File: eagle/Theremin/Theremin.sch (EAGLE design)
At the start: 50 parts, among them Q1 2N3904, Q2 2N3904, Q6 2N3904, Q7 2N3904, Q8 2N3904, U1 LM78L12, U2 LM79L12

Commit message: Work on VOLTAGE CONTROLLED AMPLIFIER section
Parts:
- added C25: 1uF, SparkFun-Passives:CAP_POLPTH2
- added C26: 0.01uF, marky-parts:CAP-5M-RADIAL
- added R29: 100K, SparkFun-Resistors:RESISTORPTH-1/4W
- added R30: 47K, SparkFun-Resistors:RESISTORPTH-1/4W
- added R32, R33, R34: 4.7M, SparkFun-Passives:RESISTOREZ
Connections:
- new net N$27: R29.2, R30.1, U3.BIAS-IN-A
- new net N$29: C25.-, R32.2, U3.B-OUT-A
- new net N$30: C25.+, R33.1
- new net N$31: C26.2, JP2.10, R33.2, R34.1
- net -12V: now also R29.1, R32.1
- net GND: now also C26.1, R34.2
- net N$24: now also R30.2
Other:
- note added: "VCA PROCESSOR"
- note added: "VOLTAGE CONTROLLED AMPLIFIER"
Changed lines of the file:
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@@
 <part name="P-5" library="supply1" deviceset="-12V" device=""/>
 <part name="SUPPLY4" library="SparkFun-Aesthetics" deviceset="5V" device="" value="12V"/>
+<part name="R30" library="SparkFun-Resistors" deviceset="RESISTOR" device="PTH-1/4W" value="47K"/>
+<part name="R29" library="SparkFun-Resistors" deviceset="RESISTOR" device="PTH-1/4W" value="100K"/>
+<part name="R32" library="SparkFun-Passives" deviceset="RESISTOR" device="EZ" value="4.7M"/>
+<part name="C25" library="SparkFun-Passives" deviceset="CAP_POL" device="PTH2" value="1uF"/>
+<part name="R33" library="SparkFun-Passives" deviceset="RESISTOR" device="EZ" value="4.7M"/>
+<part name="C26" library="marky-parts" deviceset="CAP-5M-RADIAL" device="" value="0.01uF"/>
+<part name="R34" library="SparkFun-Passives" deviceset="RESISTOR" device="EZ" value="4.7M"/>
+<part name="GND16" library="supply1" deviceset="GND" device=""/>
 </parts>
 <sheets>
@@
 <text x="45.72" y="172.72" size="1.778" layer="91">VARIABLE PITCH
 OSCILLATOR</text>
+<text x="175.26" y="43.18" size="1.778" layer="91">VCA PROCESSOR</text>
+<text x="113.03" y="97.79" size="1.778" layer="91">VOLTAGE CONTROLLED
+AMPLIFIER</text>
 </plain>
 <instances>
@@
 <instance part="P-5" gate="1" x="132.08" y="11.43"/>
 <instance part="SUPPLY4" gate="G$1" x="95.25" y="19.05"/>
+<instance part="R30" gate="G$1" x="128.27" y="41.91" rot="R270"/>
+<instance part="R29" gate="G$1" x="120.65" y="52.07"/>
+<instance part="R32" gate="G$1" x="114.3" y="62.23" rot="R90"/>
+<instance part="C25" gate="G$1" x="90.17" y="59.69" rot="R180"/>
+<instance part="R33" gate="G$1" x="90.17" y="49.53" rot="R270"/>
+<instance part="C26" gate="G$1" x="82.55" y="41.91" rot="R90"/>
+<instance part="R34" gate="G$1" x="82.55" y="34.29" rot="R180"/>
+<instance part="GND16" gate="1" x="73.66" y="30.48"/>
 </instances>
 <busses>
@@
 <pinref part="GND15" gate="1" pin="GND"/>
 </segment>
+<segment>
+<pinref part="C26" gate="G$1" pin="1"/>
+<wire x1="78.74" y1="41.91" x2="76.2" y2="41.91" width="0.1524" layer="91"/>
+<wire x1="76.2" y1="41.91" x2="76.2" y2="38.1" width="0.1524" layer="91"/>
+<pinref part="R34" gate="G$1" pin="2"/>
+<wire x1="76.2" y1="38.1" x2="76.2" y2="34.29" width="0.1524" layer="91"/>
+<wire x1="76.2" y1="34.29" x2="77.47" y2="34.29" width="0.1524" layer="91"/>
+<wire x1="76.2" y1="38.1" x2="73.66" y2="38.1" width="0.1524" layer="91"/>
+<wire x1="73.66" y1="38.1" x2="73.66" y2="33.02" width="0.1524" layer="91"/>
+<pinref part="GND16" gate="1" pin="GND"/>
+<junction x="76.2" y="38.1"/>
+</segment>
 </net>
 <net name="N$7" class="0">
@@
 <pinref part="P-4" gate="1" pin="-12V"/>
 <wire x1="143.51" y1="55.88" x2="143.51" y2="53.34" width="0.1524" layer="91"/>
-<wire x1="143.51" y1="53.34" x2="143.51" y2="44.45" width="0.1524" layer="91"/>
+<wire x1="143.51" y1="53.34" x2="143.51" y2="48.26" width="0.1524" layer="91"/>
+<wire x1="143.51" y1="48.26" x2="143.51" y2="44.45" width="0.1524" layer="91"/>
 <wire x1="143.51" y1="53.34" x2="193.04" y2="53.34" width="0.1524" layer="91"/>
 <wire x1="193.04" y1="53.34" x2="204.47" y2="76.2" width="0.1524" layer="91"/>
@@
 <pinref part="JP1" gate="G$1" pin="5"/>
 <junction x="143.51" y="53.34"/>
+<pinref part="R32" gate="G$1" pin="1"/>
+<wire x1="114.3" y1="57.15" x2="114.3" y2="52.07" width="0.1524" layer="91"/>
+<pinref part="R29" gate="G$1" pin="1"/>
+<wire x1="114.3" y1="52.07" x2="114.3" y2="48.26" width="0.1524" layer="91"/>
+<wire x1="115.57" y1="52.07" x2="114.3" y2="52.07" width="0.1524" layer="91"/>
+<junction x="114.3" y="52.07"/>
+<wire x1="143.51" y1="48.26" x2="114.3" y2="48.26" width="0.1524" layer="91"/>
+<junction x="143.51" y="48.26"/>
 </segment>
 <segment>
@@
 <wire x1="198.12" y1="52.07" x2="160.02" y2="52.07" width="0.1524" layer="91"/>
 <junction x="160.02" y="52.07"/>
-<wire x1="160.02" y1="52.07" x2="114.3" y2="52.07" width="0.1524" layer="91"/>
+<wire x1="160.02" y1="52.07" x2="151.13" y2="52.07" width="0.1524" layer="91"/>
+<wire x1="151.13" y1="52.07" x2="151.13" y2="36.83" width="0.1524" layer="91"/>
+<wire x1="151.13" y1="36.83" x2="128.27" y2="36.83" width="0.1524" layer="91"/>
 <pinref part="D5" gate="G$1" pin="C"/>
 <wire x1="163.83" y1="58.42" x2="160.02" y2="58.42" width="0.1524" layer="91"/>
 <junction x="160.02" y="58.42"/>
+<pinref part="R30" gate="G$1" pin="2"/>
 </segment>
 </net>
@@
 </segment>
 </net>
+<net name="N$27" class="0">
+<segment>
+<pinref part="U3" gate="G$1" pin="BIAS-IN-A"/>
+<pinref part="R30" gate="G$1" pin="1"/>
+<wire x1="130.81" y1="78.74" x2="128.27" y2="78.74" width="0.1524" layer="91"/>
+<wire x1="128.27" y1="78.74" x2="128.27" y2="52.07" width="0.1524" layer="91"/>
+<pinref part="R29" gate="G$1" pin="2"/>
+<wire x1="128.27" y1="52.07" x2="128.27" y2="46.99" width="0.1524" layer="91"/>
+<wire x1="125.73" y1="52.07" x2="128.27" y2="52.07" width="0.1524" layer="91"/>
+<junction x="128.27" y="52.07"/>
+</segment>
+</net>
+<net name="N$29" class="0">
+<segment>
+<pinref part="U3" gate="G$1" pin="B-OUT-A"/>
+<wire x1="130.81" y1="68.58" x2="114.3" y2="68.58" width="0.1524" layer="91"/>
+<wire x1="114.3" y1="68.58" x2="90.17" y2="68.58" width="0.1524" layer="91"/>
+<wire x1="90.17" y1="68.58" x2="90.17" y2="64.77" width="0.1524" layer="91"/>
+<pinref part="R32" gate="G$1" pin="2"/>
+<wire x1="114.3" y1="67.31" x2="114.3" y2="68.58" width="0.1524" layer="91"/>
+<junction x="114.3" y="68.58"/>
+<pinref part="C25" gate="G$1" pin="-"/>
+</segment>
+</net>
+<net name="N$30" class="0">
+<segment>
+<pinref part="R33" gate="G$1" pin="1"/>
+<pinref part="C25" gate="G$1" pin="+"/>
+<wire x1="90.17" y1="54.61" x2="90.17" y2="57.15" width="0.1524" layer="91"/>
+</segment>
+</net>
+<net name="N$31" class="0">
+<segment>
+<pinref part="R33" gate="G$1" pin="2"/>
+<pinref part="JP2" gate="G$1" pin="10"/>
+<wire x1="90.17" y1="44.45" x2="90.17" y2="41.91" width="0.1524" layer="91"/>
+<pinref part="C26" gate="G$1" pin="2"/>
+<wire x1="90.17" y1="41.91" x2="90.17" y2="34.29" width="0.1524" layer="91"/>
+<wire x1="90.17" y1="34.29" x2="90.17" y2="15.24" width="0.1524" layer="91"/>
+<wire x1="86.36" y1="41.91" x2="90.17" y2="41.91" width="0.1524" layer="91"/>
+<pinref part="R34" gate="G$1" pin="1"/>
+<wire x1="87.63" y1="34.29" x2="90.17" y2="34.29" width="0.1524" layer="91"/>
+<junction x="90.17" y="41.91"/>
+<junction x="90.17" y="34.29"/>
+</segment>
+</net>

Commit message: Finish VOLTAGE CONTROLLED AMP, add DETECTOR
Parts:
- added C23: 4700pF, SparkFun-Capacitors:CAPPTH
- added C24: 3300pF, SparkFun-Capacitors:CAPPTH
- added D4: (no value), SparkFun-DiscreteSemi:DIODE1N4148
- added R23: 10K, SparkFun-Resistors:RESISTORPTH-1/4W
- added R24: 4.7K, SparkFun-Resistors:RESISTORPTH-1/4W
- added R25: 330K, SparkFun-Resistors:RESISTORPTH-1/4W
- added R26, R31: 4.7M, SparkFun-Passives:RESISTOREZ
- added R27, R28: 150K, SparkFun-Resistors:RESISTORPTH-1/4W
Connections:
- new net N$32: C24.2, R31.2, U3.B-IN-A, U3.OUT-A
- new net N$33: R27.2, U3.DIODE-BIAS-A
- new net N$34: JP2.9, R27.1
- new net N$35: JP2.7, R28.1
- new net N$36: R25.2, R26.2, R28.2, U3.IN-MINUS-A
- new net N$37: C23.1, JP1.7, R23.2, R24.1
- new net N$38: C23.2, D4.C, R24.2
- new net VNEG: R25.1
- net GND: now also C24.1, R26.1, R31.1
- net N$20: now also D4.A, R23.1
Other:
- note added: "DETECTOR"
- note removed: "Volume Antenna Circuit"

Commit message: work on POWER SUPPLY
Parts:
- added C21, C22: 0.1uF, SparkFun-Capacitors:CAPPTH
- added JP3: POWER IN, SparkFun-Connectors:M02LOCK
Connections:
- new net N$39: JP2.1, JP3.2
- net -12V: no longer JP2.3
- net 5V: now also C21.1, U1.VOUT
- net GND: now also C21.2, C22.1, JP3.1
- net N$14: now also JP2.2
- net VNEG: now also C22.2, JP2.3, U2.VOUT
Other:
- note added: "POWER SUPPLY"
- note removed: "Power Supply"
- moved on the sheet: C25, C26, JP2, R33, R34

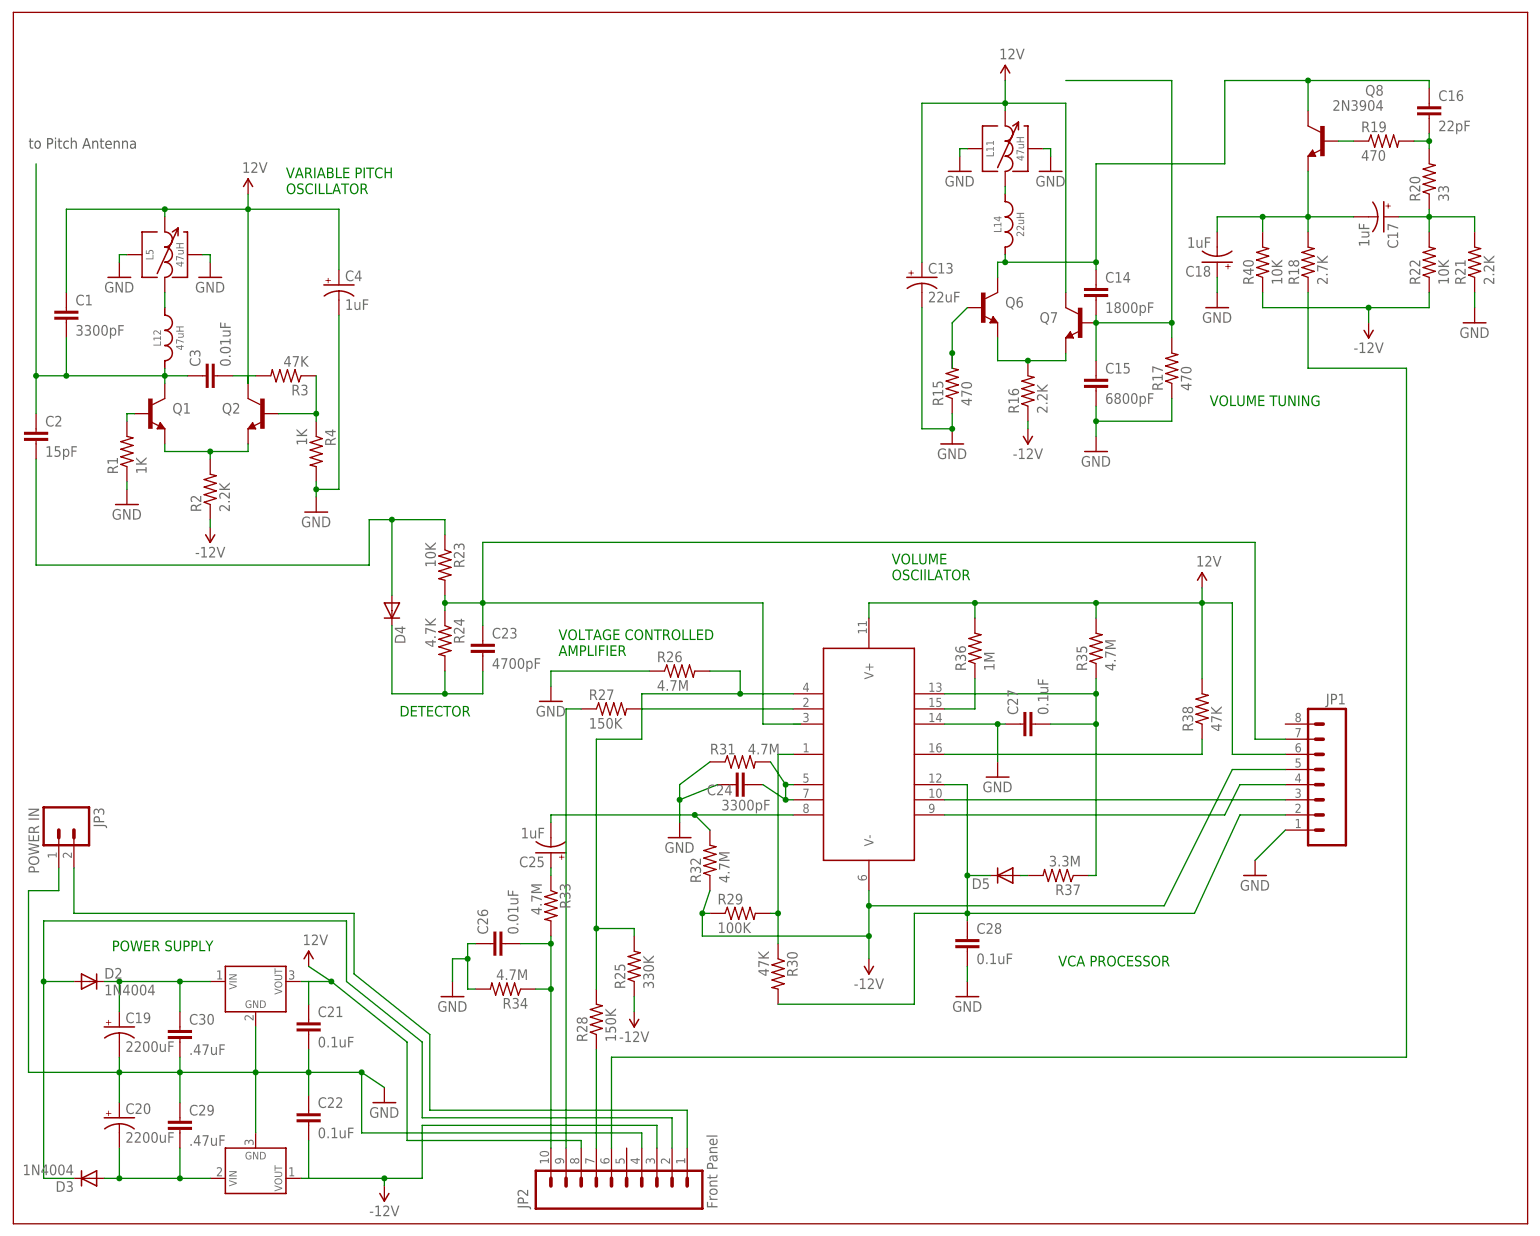
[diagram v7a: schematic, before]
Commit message: Add the FIXED PITCH OSCILLATOR curcuit
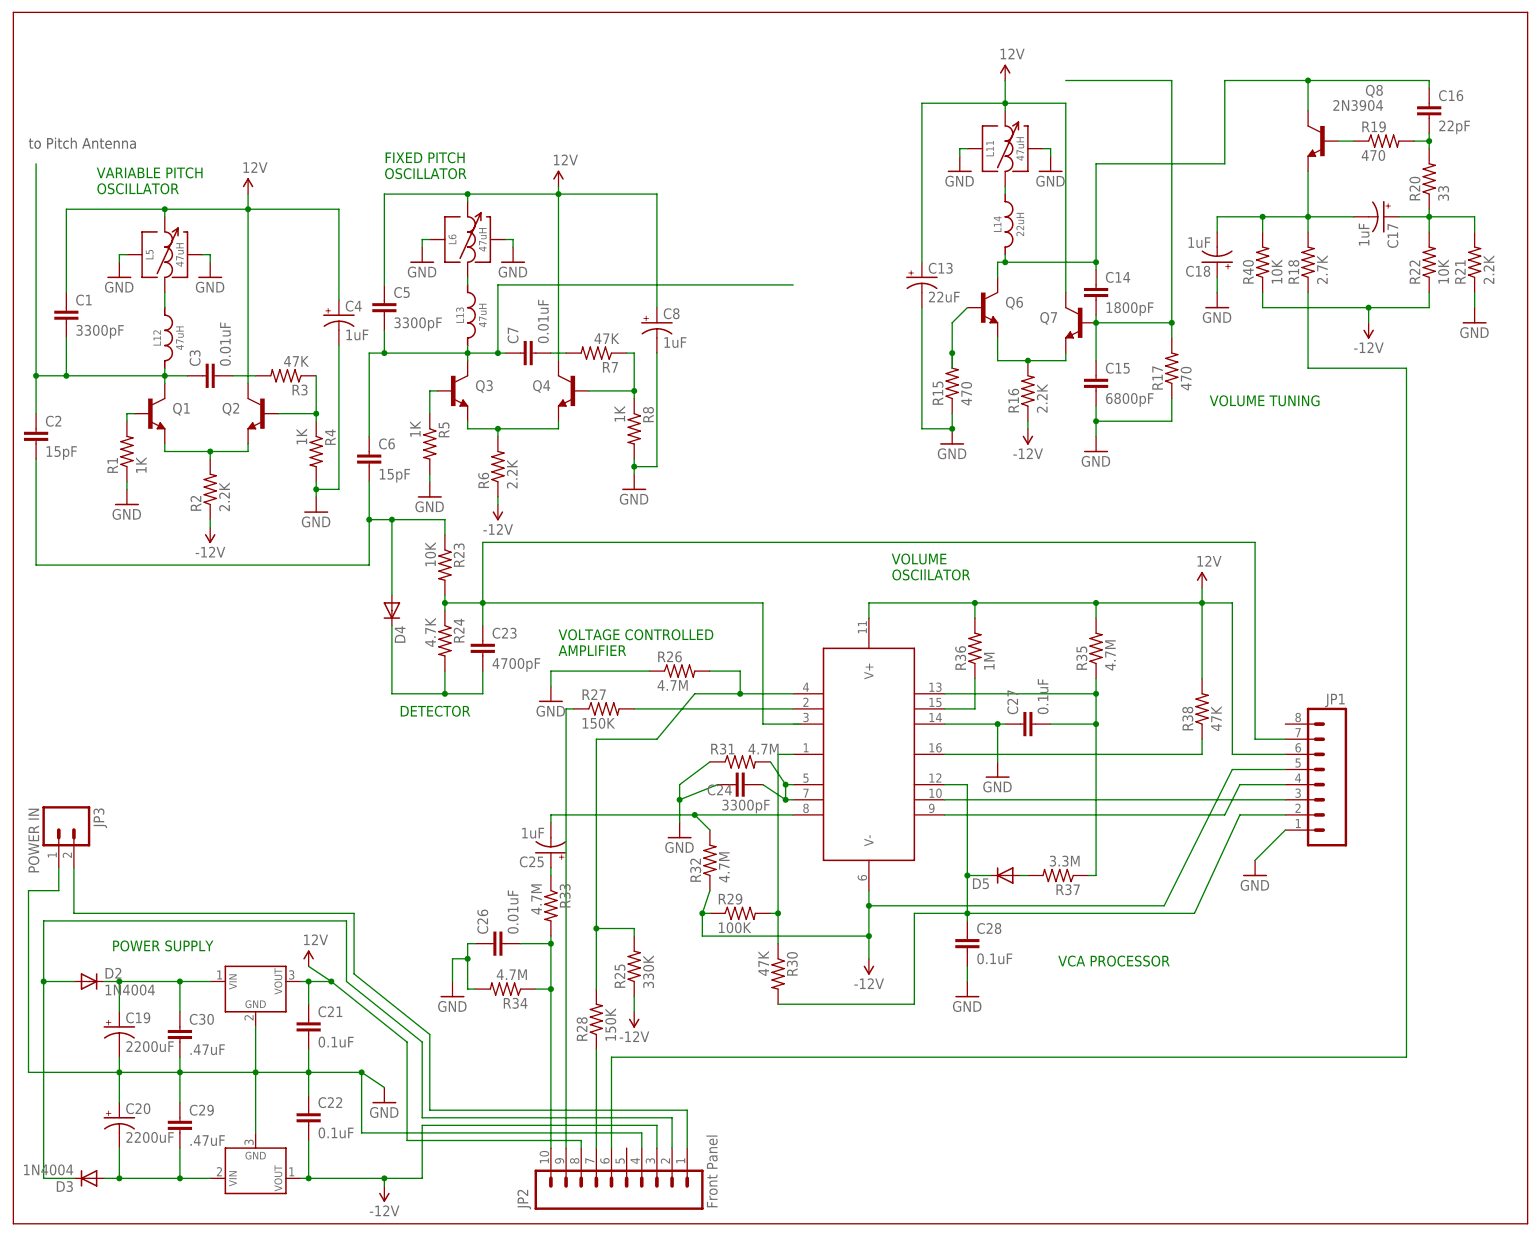
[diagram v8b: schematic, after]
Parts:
- added C5: 3300pF, marky-parts:CAP-9M-RADIAL
- added C6: 15pF, SparkFun-Capacitors:CAPPTH
- added C7: 0.01uF, marky-parts:CAP-5M-RADIAL
- added C8: 1uF, SparkFun-Passives:CAP_POLPTH2
- added L13: 47uH, marky-parts:DELEVAN-FIXED-INDUCTOR
- added L6: 47uH, marky-parts:SLOT-TEN-SIMPLE
- added Q3, Q4: 2N3904, transistor:2N3904
- added R5, R8: 1K, SparkFun-Resistors:RESISTORPTH-1/4W
- added R6: 2.2K, SparkFun-Resistors:RESISTORPTH-1/4W
- added R7: 47K, SparkFun-Resistors:RESISTORPTH-1/4W
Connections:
- new net N$40: C3.2, R3.2
- new net N$41: C5.2, C6.1, C7.1, L13.P$2, Q3.C
- new net N$42: Q3.B, R5.1
- new net N$43: Q3.E, Q4.E, R6.2
- new net N$44: L13.P$1, L6.OUT$2
- new net N$46: C7.2, R7.2
- new net N$48: Q4.B, R7.1, R8.1
- net 5V: now also C5.1, C8.+, L6.IN$1, Q4.C; no longer C3.2, R3.2
- net GND: now also C8.-, L6.P$1, L6.P$2, R5.2, R8.2
- net N$20: now also C6.2
- net VNEG: now also R6.1
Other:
- note added: "FIXED PITCH OSCILLATOR"
- moved on the sheet: C4, R27
